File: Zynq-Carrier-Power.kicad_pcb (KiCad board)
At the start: 2 copper layers, 49 x 41 mm, 34 parts, among them J1 Zynq_SoM, J10 Barrel_Jack_MountingPin, J2 B2B-PH-K-S, J3 USB_C_Receptacle_USB2.0_16P, J4 Conn_01x03, J5 Conn_01x03, J6 Conn_01x03, J7 Conn_01x02, J8 Conn_01x02, J9 Conn_01x03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

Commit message: Modified Vias and Reorganized
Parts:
- moved C1 3.03 mm to (130.4, 121.0)
- moved C2 3.03 mm to (131.9, 121.0)
- moved L1 0.70 mm to (126.5, 112.6)
- moved J5 0.21 mm to (139.2, 123.6)
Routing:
- net GND: track 16.0 -> 44.4 mm
- net +5V: track 36.7 -> 39.1 mm
- net Net-(U1-PMID): track 3.61 -> 1.97 mm
- net /SDA: vias 1 -> 0
- net /SW: vias 14 -> 15

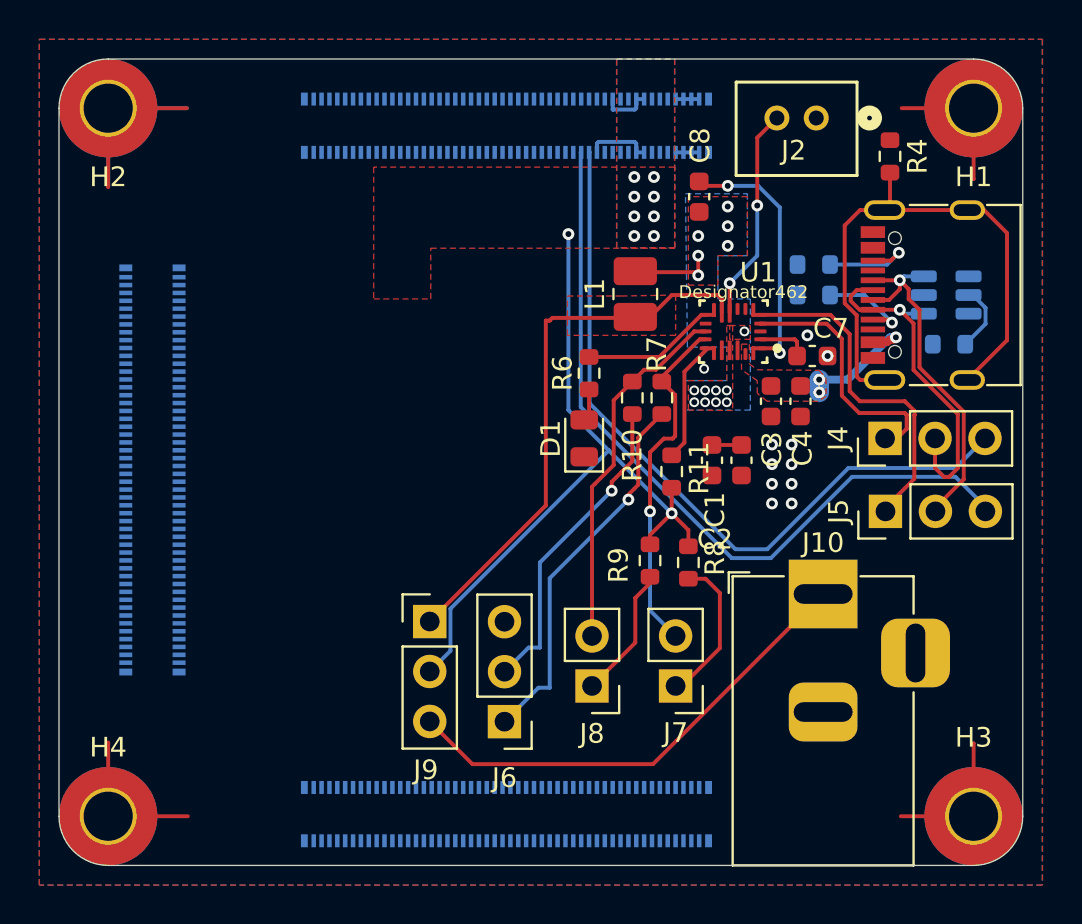
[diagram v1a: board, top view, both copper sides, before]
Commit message: Fixed More PCB Errors
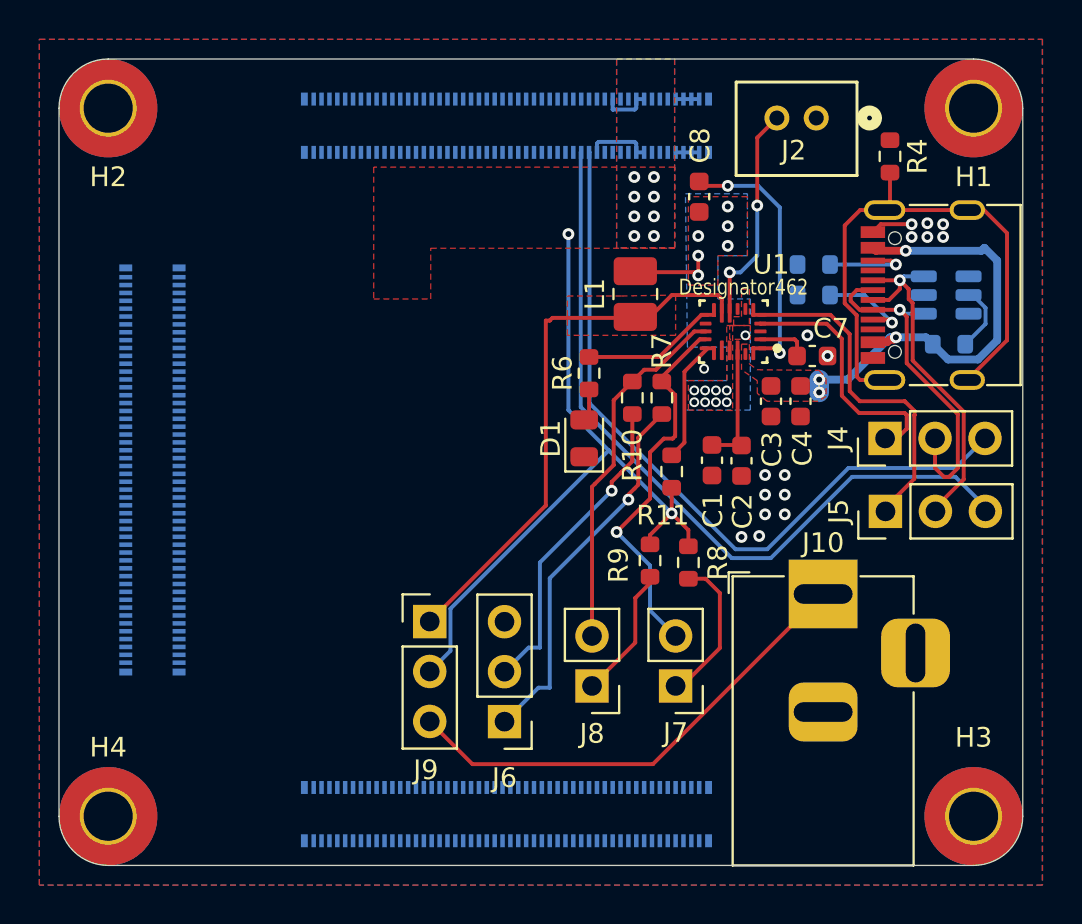
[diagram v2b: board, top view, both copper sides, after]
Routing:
- net GND: track 44.4 -> 8.12 mm, vias 11 -> 17
- net V_USB: track 6.71 -> 23.5 mm, vias 3 -> 4
- net Net-(U1-PMID): track 1.97 -> 6.89 mm
- net /SCL: track 17.8 -> 19.2 mm
- net Net-(J3-CC2): track 5.23 -> 4.60 mm

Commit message: Fixed most DRC errors
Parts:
- moved J1 2.28 mm to (143.6, 100.1)
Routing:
- net GND: track 8.12 -> 2.14 mm
- net /USB_SOM_D-: track 38.3 -> 39.6 mm
- net /USB_SOM_D+: track 39.1 -> 40.4 mm
- net +5V: track 39.1 -> 37.9 mm

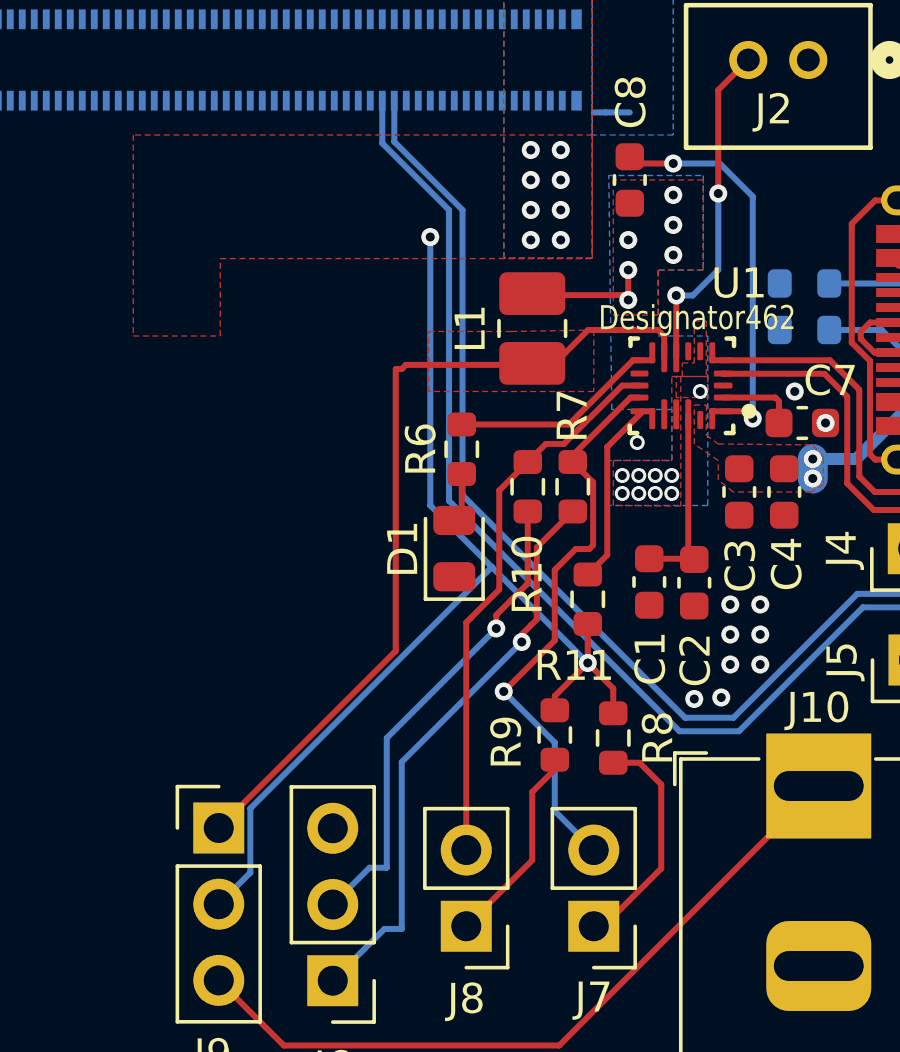
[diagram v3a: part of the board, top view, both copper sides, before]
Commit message: Modified VREG_OUT & Silkscreen
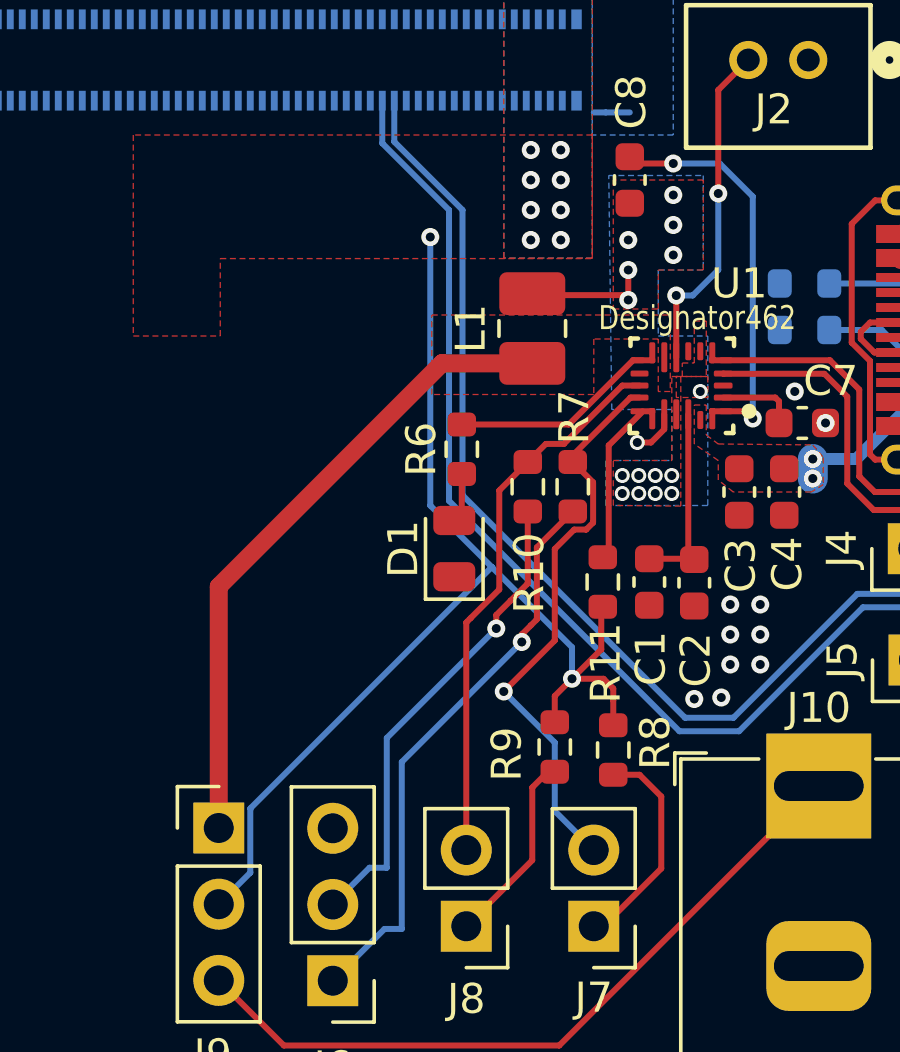
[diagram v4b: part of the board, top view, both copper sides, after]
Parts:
- moved R11 0.76 mm to (128.9, 121.0)
- moved R9 0.40 mm to (127.3, 126.5)
- moved R8 0.40 mm to (129.2, 126.6)
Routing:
- net VREG_OUT: track 28.0 -> 21.6 mm
- net +5V: track 37.9 -> 40.1 mm
- net GND: track 2.14 -> 3.72 mm
- net /~{CSn}: track 6.20 -> 5.42 mm

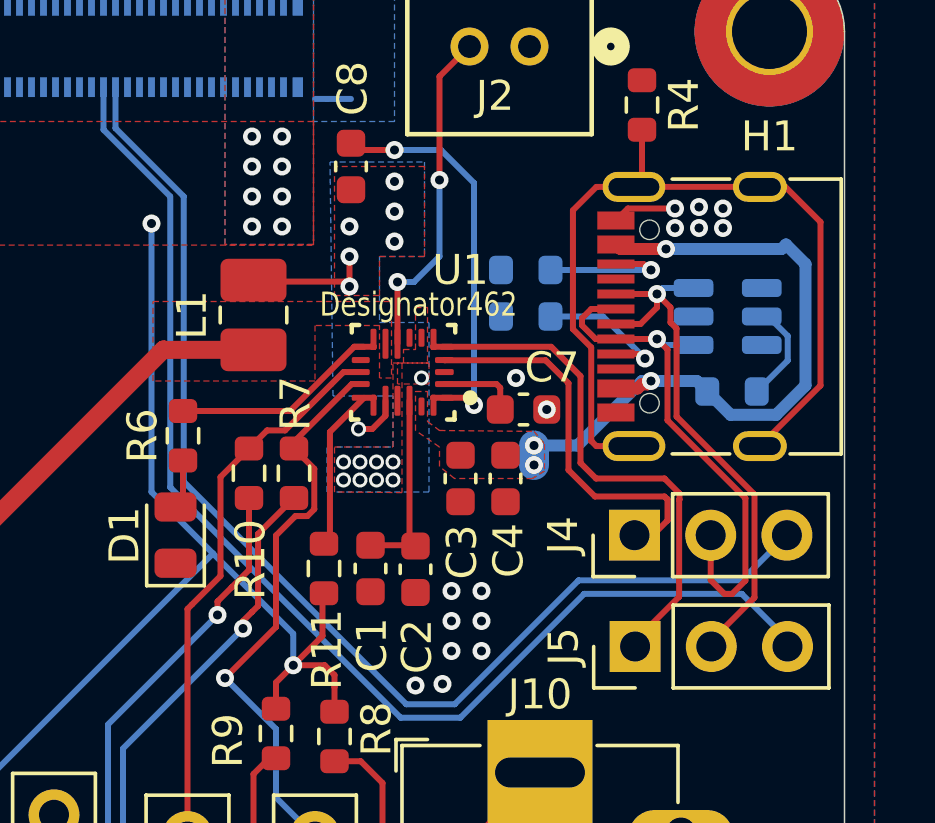
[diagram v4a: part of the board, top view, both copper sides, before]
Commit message: edited DRC constraints
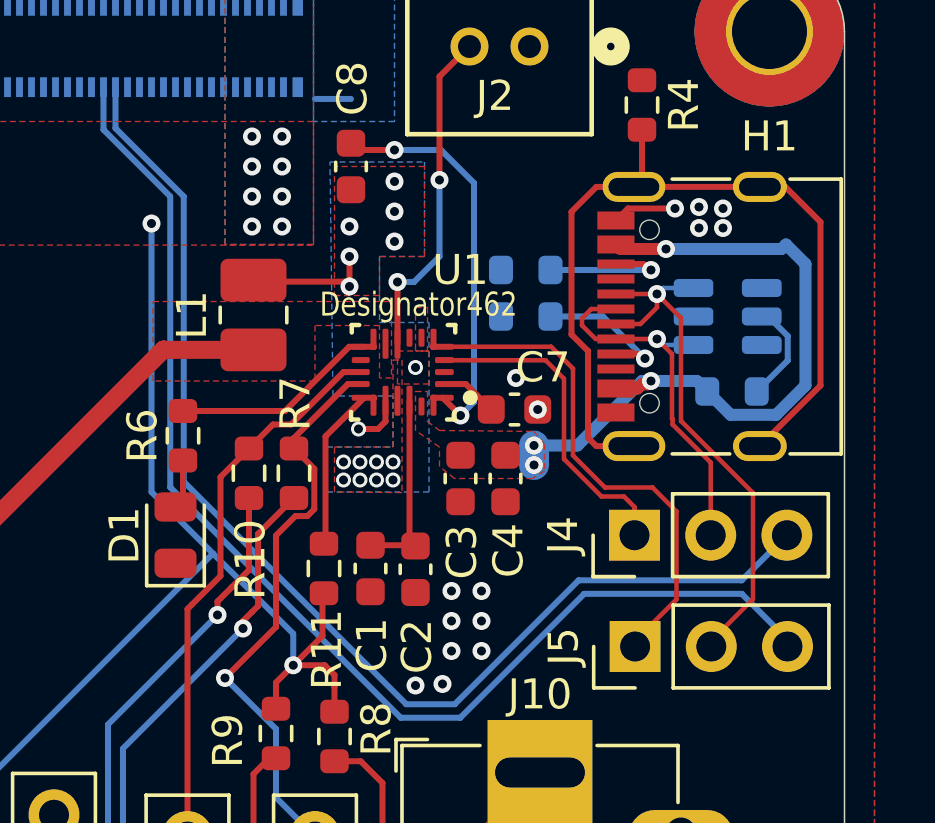
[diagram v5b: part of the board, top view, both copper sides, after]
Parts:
- moved C7 0.30 mm to (135.2, 115.7)
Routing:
- net /USB_D-: track 17.8 -> 12.8 mm
- net /USB_POW_D-: track 13.1 -> 10.9 mm
- net Net-(U1-REGN): track 2.64 -> 1.91 mm
- net GND: track 3.72 -> 3.83 mm, vias 17 -> 16

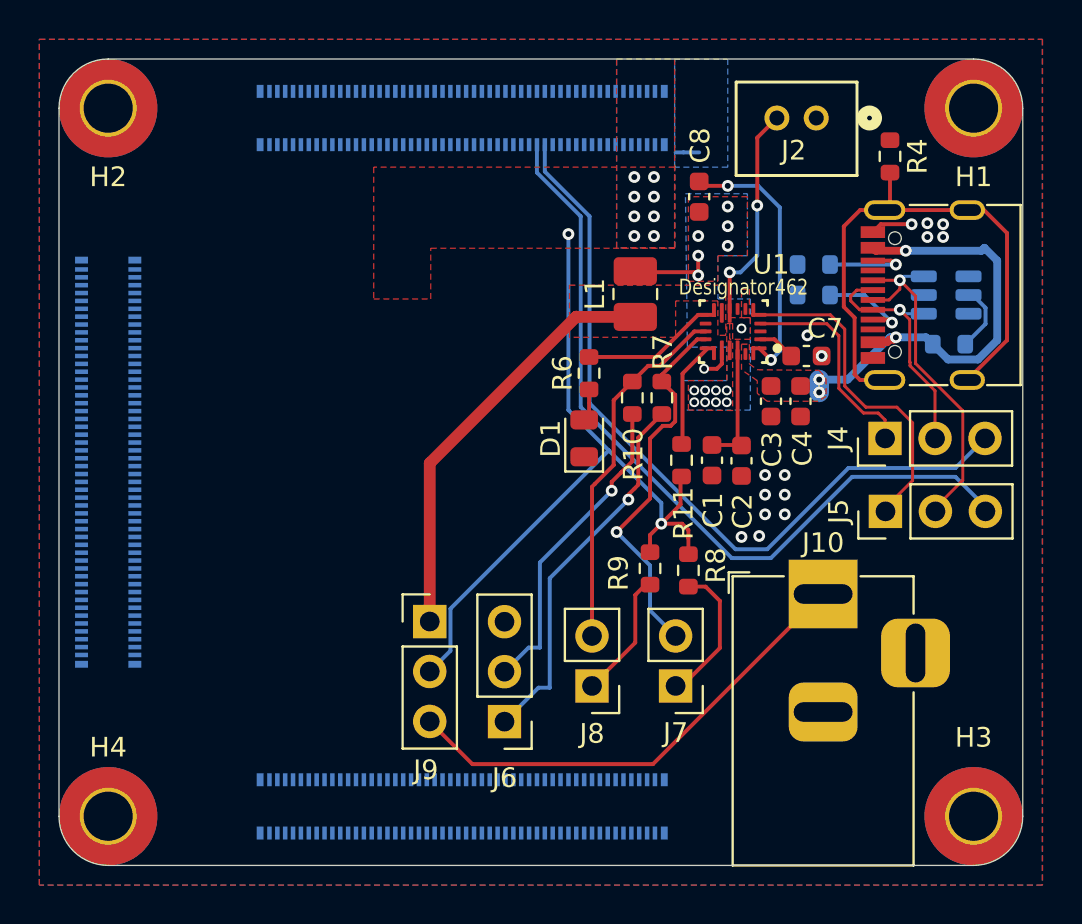
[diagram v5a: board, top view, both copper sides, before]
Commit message: Modified PCB & Schematic for new constraints
Modifications are not done yet. Some errors are still present
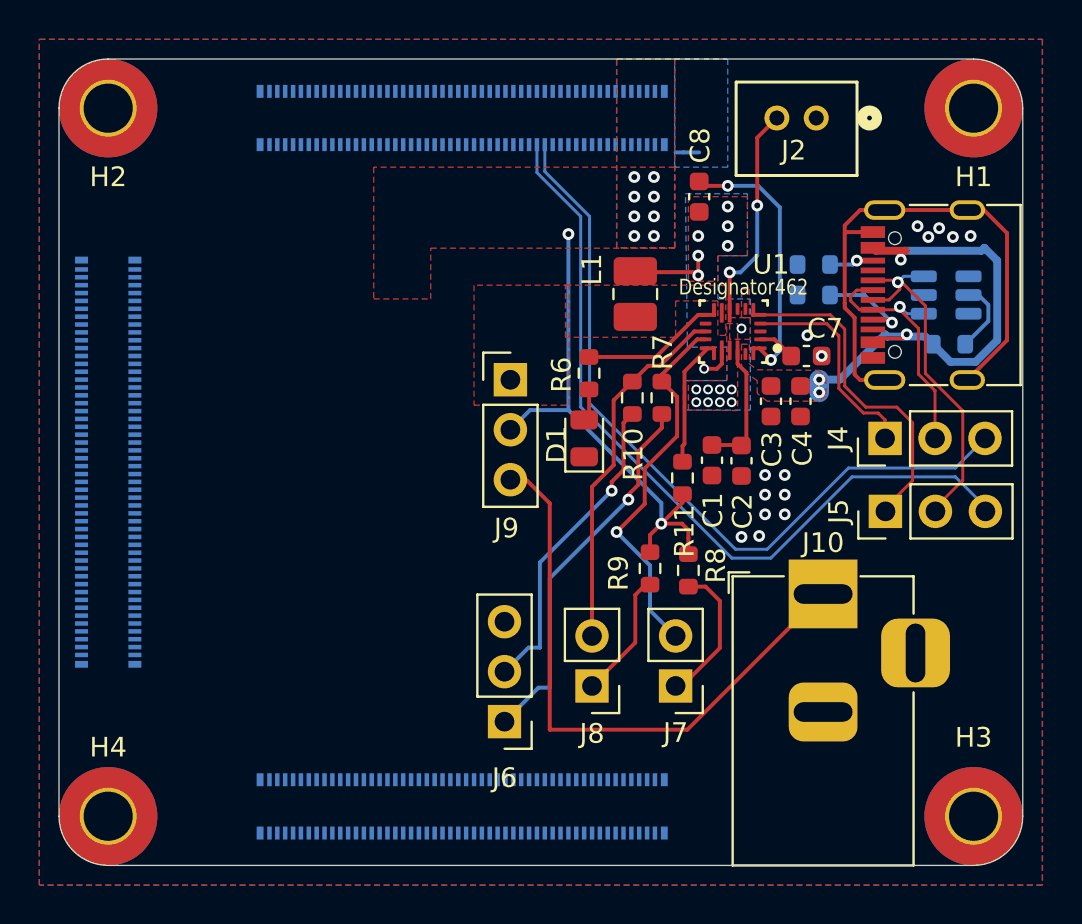
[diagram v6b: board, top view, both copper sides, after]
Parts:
- removed R4: 1M, Resistor_SMD:R_0603_1608Metric
- moved J9 13.0 mm to (120.2, 117.0)
- moved R11 0.90 mm to (128.9, 121.9)
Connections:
- J3 pad S1: Net-(J3-SHIELD) -> GND
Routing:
- net Net-(J3-SHIELD): track 28.9 -> 0.00 mm
- net GND: track 3.83 -> 30.3 mm
- net VREG_OUT: track 21.6 -> 0.00 mm
- net +5V: track 40.1 -> 27.6 mm
- net Vps: track 24.5 -> 30.0 mm
- net Net-(J3-CC2): track 4.60 -> 1.45 mm
- net V_USB: track 23.5 -> 24.9 mm
- net /~{CSn}: track 5.42 -> 6.30 mm

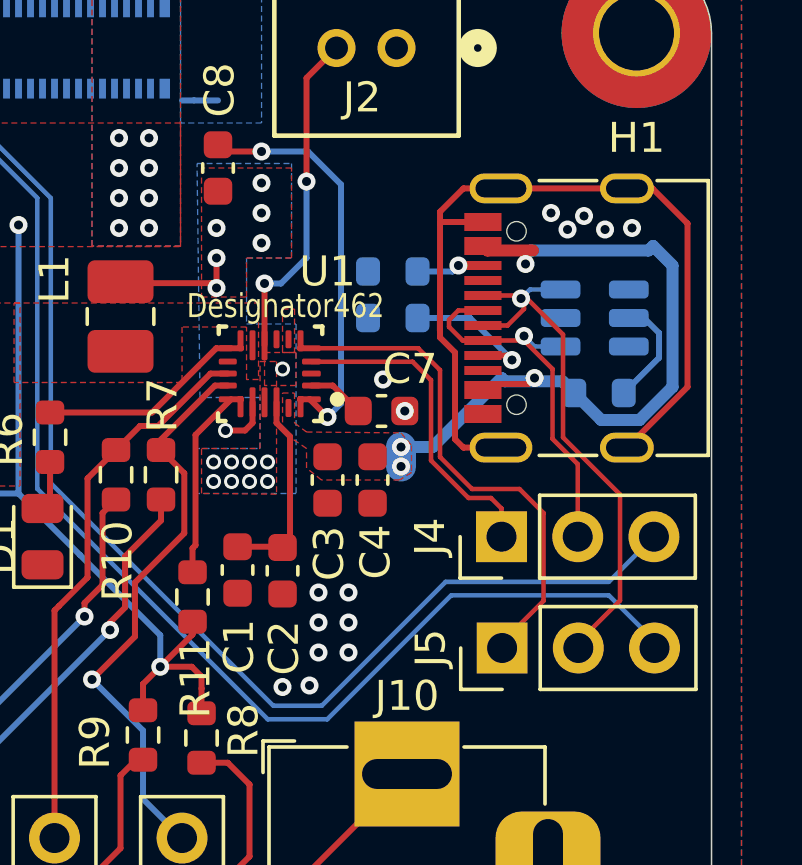
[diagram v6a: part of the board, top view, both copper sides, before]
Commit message: Updated V_USB Connections
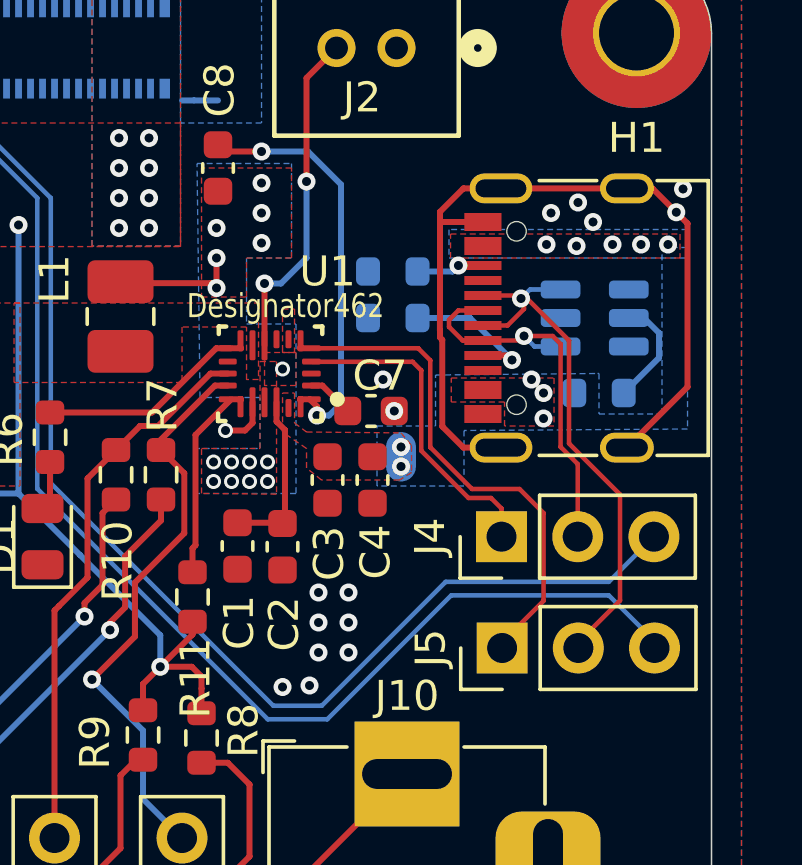
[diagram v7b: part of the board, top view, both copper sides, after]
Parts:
- moved C1 0.80 mm to (130.4, 120.2)
- moved C2 0.80 mm to (131.9, 120.3)
- moved C7 0.35 mm to (134.9, 115.7)
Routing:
- net V_USB: track 24.9 -> 0.65 mm, vias 4 -> 10
- net Net-(U1-PMID): track 7.10 -> 6.16 mm
- net /USB_D-: track 13.0 -> 13.5 mm
- added copper zone on B.Cu, net V_USB
